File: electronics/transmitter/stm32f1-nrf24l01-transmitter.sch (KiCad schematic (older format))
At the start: 34 parts, among them K1 CONN_3, K10 CONN_3, K11 CONN_3, K12 UART, K2 CONN_3, K3 CONN_3, K4 CONN_3, K5 CONN_3, K6 CONN_3, K7 CONN_3, K8 CONN_3, K9 CONN_3, P1 Charge, P2 LED, P3 PWR-BAT, P4 PWR-IN, P5 Buzzer, P6 Meter, Q1 BC547B, SW1 ON/OFF, U1 LIPO_CHARGER_+_PROTECTION, U2 STM32F103C8T6_DEV_BOARD, U3 NRF24L01P

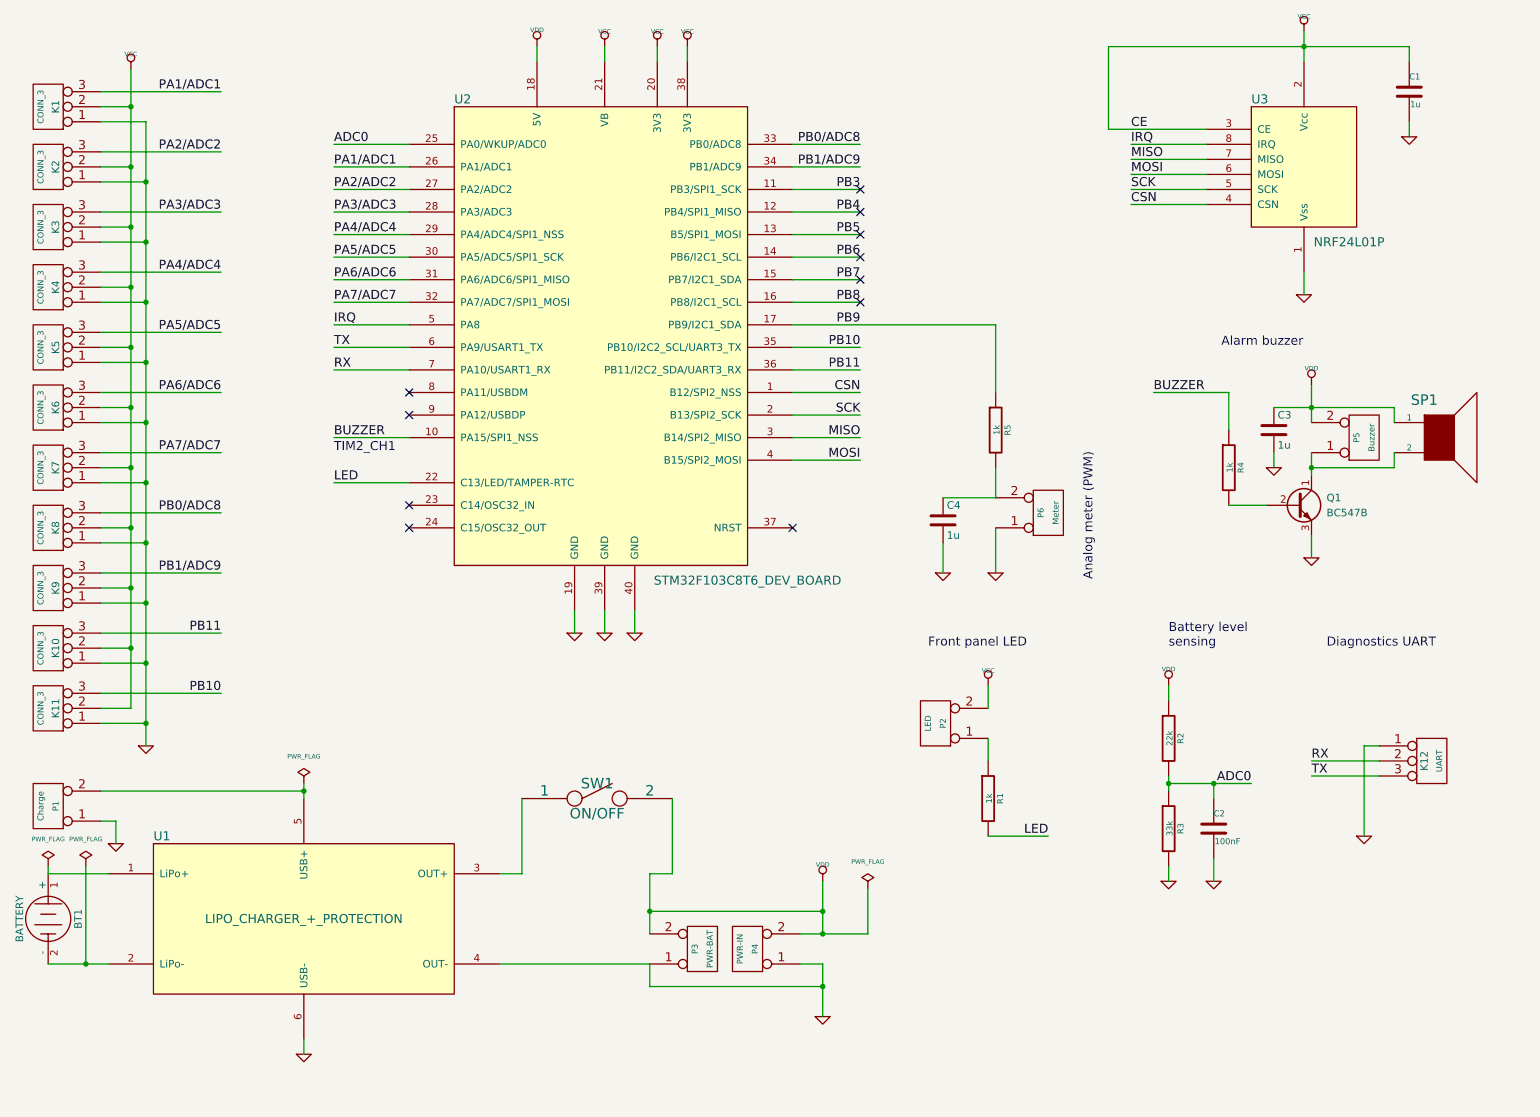
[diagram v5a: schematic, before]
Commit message: Add info about Airtronics meter
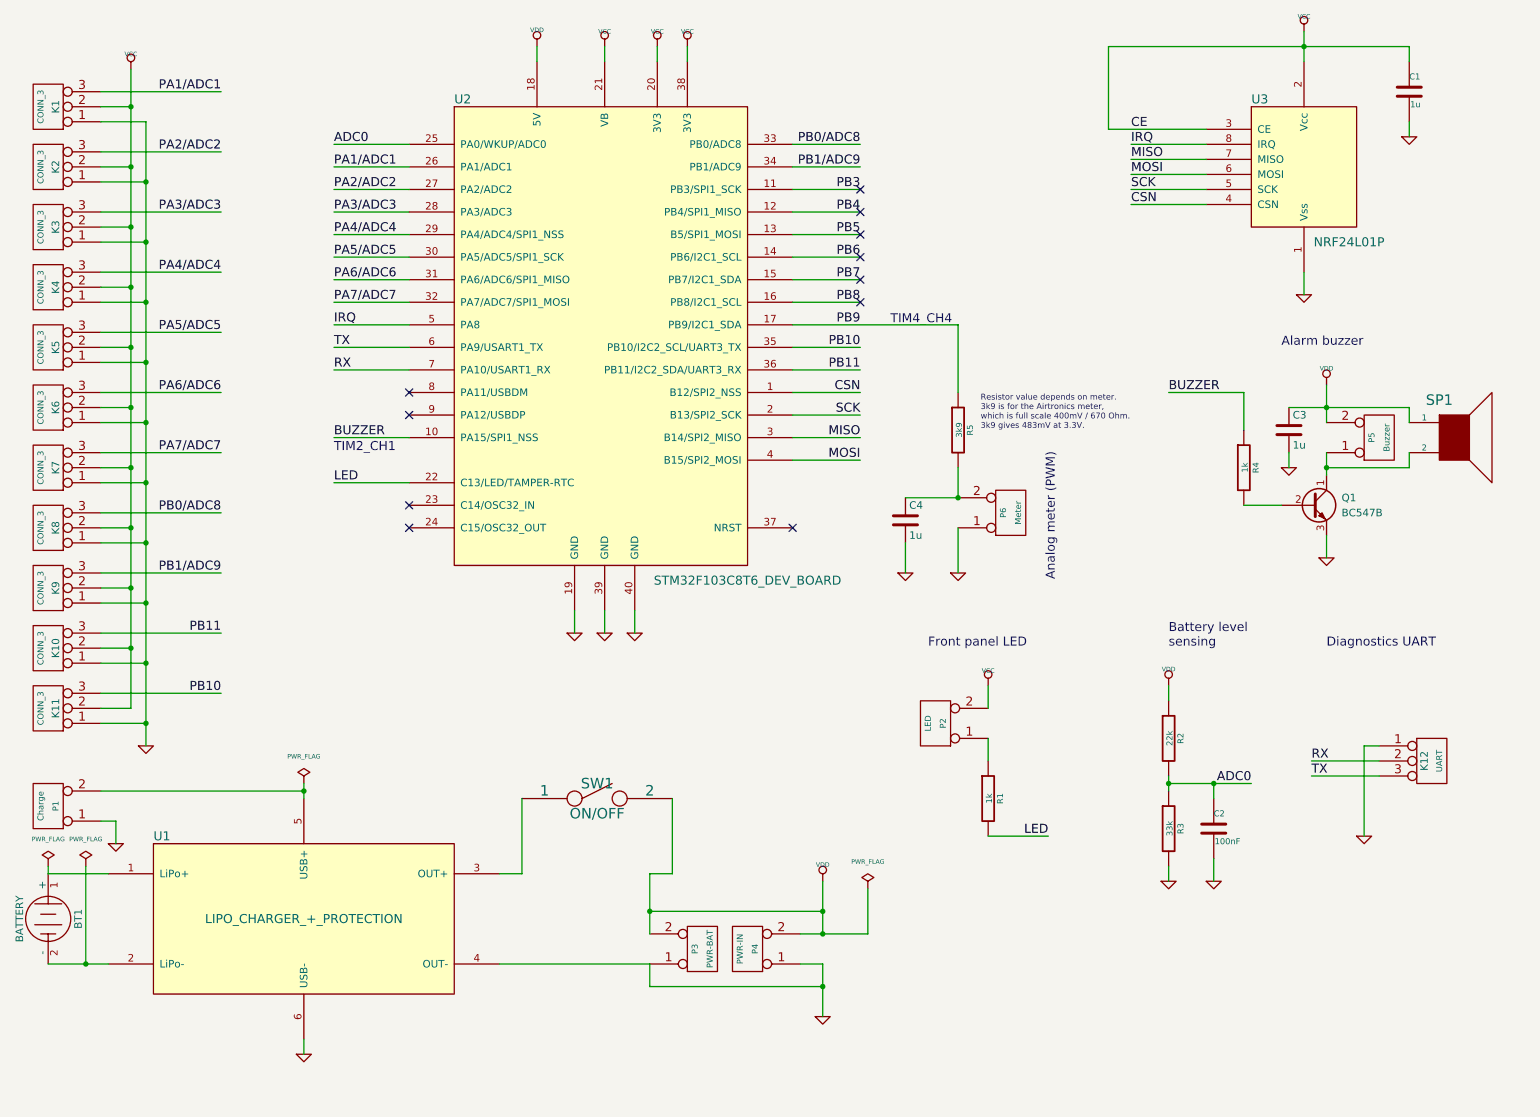
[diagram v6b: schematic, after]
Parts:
- R5: value 1k -> 3k9
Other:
- note added: "Resistor value depends on meter. \n3k9 is for the Airtronics meter, \nwhich is full scale 400mV / 670 Ohm.\n3k9 gives 483mV at 3.3V."
- note added: "TIM4_CH4"
- moved on the sheet: C3, C4, P5, P6, Q1, R4, R5, SP1

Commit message: Remove values on connectors, fix-up meter resistor
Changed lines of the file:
@@
 	10350 1350 10350 1450
 Wire Wire Line
-	9650 750  9650 850
-Wire Wire Line
-	9650 850  9650 950
+	9650 750  9650 950
 Wire Wire Line
 	10350 850  10350 950
@@
 	8750 5100 8750 5200
 Wire Wire Line
-	8750 5700 8750 5750
-Wire Wire Line
-	8750 5750 8750 5800
+	8750 5700 8750 5800
 Wire Wire Line
 	8750 6300 8750 6400
 Wire Wire Line
-	8750 5750 9050 5750
-Wire Wire Line
-	9050 5750 9300 5750
+	8750 5750 9300 5750
 Connection ~ 8750 5750
 Wire Wire Line
@@
 	1950 5350 1650 5350
 Wire Wire Line
-	1950 1350 1950 1750
-Wire Wire Line
-	1950 1750 1950 2150
-Wire Wire Line
-	1950 2150 1950 2550
-Wire Wire Line
-	1950 2550 1950 2950
-Wire Wire Line
-	1950 2950 1950 3350
-Wire Wire Line
-	1950 3350 1950 3750
-Wire Wire Line
-	1950 3750 1950 4150
-Wire Wire Line
-	1950 4150 1950 4550
-Wire Wire Line
-	1950 4550 1950 4950
-Wire Wire Line
-	1950 4950 1950 5350
-Wire Wire Line
-	1950 5350 1950 5500
+	1950 1350 1950 5500
 Wire Wire Line
 	1650 4950 1950 4950
@@
 	9800 4100 9800 4250
 Wire Wire Line
-	9800 3550 9800 3650
-Wire Wire Line
-	9800 3650 9800 3700
+	9800 3550 9800 3700
 Wire Wire Line
 	9250 3900 9500 3900
@@
 	9250 3150 8750 3150
 Wire Wire Line
-	9800 3100 9800 3250
-Wire Wire Line
-	9800 3250 9800 3350
+	9800 3100 9800 3350
 Wire Wire Line
 	3200 3450 3700 3450
@@
 	1650 5800 3000 5800
 Wire Wire Line
-	3000 5750 3000 5800
-Wire Wire Line
-	3000 5800 3000 5850
-Wire Wire Line
-	1300 6950 1550 6950
-Wire Wire Line
-	1550 6950 1700 6950
+	3000 5750 3000 5850
+Wire Wire Line
+	1300 6950 1700 6950
 Wire Wire Line
 	1300 6350 1700 6350
@@
 	1850 5250 1650 5250
 Wire Wire Line
-	1850 1000 1850 1250
-Wire Wire Line
-	1850 1250 1850 1650
-Wire Wire Line
-	1850 1650 1850 2050
-Wire Wire Line
-	1850 2050 1850 2450
-Wire Wire Line
-	1850 2450 1850 2850
-Wire Wire Line
-	1850 2850 1850 3250
-Wire Wire Line
-	1850 3250 1850 3650
-Wire Wire Line
-	1850 3650 1850 4050
-Wire Wire Line
-	1850 4050 1850 4450
-Wire Wire Line
-	1850 4450 1850 4850
-Wire Wire Line
-	1850 4850 1850 5250
+	1850 1000 1850 5250
 Wire Wire Line
 	1650 4850 1850 4850
@@
 Connection ~ 1850 1250
 Wire Wire Line
-	6300 6750 6450 6750
-Wire Wire Line
-	6450 6750 6750 6750
-Wire Wire Line
-	6450 6400 6450 6600
-Wire Wire Line
-	6450 6600 6450 6750
+	6300 6750 6750 6750
+Wire Wire Line
+	6450 6400 6450 6750
 Wire Wire Line
 	6300 6950 6450 6950
 Wire Wire Line
-	6450 6950 6450 7100
-Wire Wire Line
-	6450 7100 6450 7300
+	6450 6950 6450 7300
 Wire Wire Line
 	6750 6750 6750 6450
@@
 	5450 6350 5300 6350
 Wire Wire Line
-	5300 6350 5300 6600
-Wire Wire Line
-	5300 6600 5300 6750
+	5300 6350 5300 6750
 Wire Wire Line
 	5550 850  5550 950
 Wire Wire Line
-	8350 850  9650 850
-Wire Wire Line
-	9650 850  10350 850
+	8350 850  10350 850
 Wire Wire Line
 	8350 850  8350 1400
@@
 Connection ~ 6450 7100
 Wire Wire Line
-	9550 3250 9800 3250
-Wire Wire Line
-	9800 3250 10350 3250
+	9550 3250 10350 3250
 Wire Wire Line
 	10350 3250 10350 3350
@@
 $EndComp
 $Comp
-L VCC #PWR?
+L VCC #PWR030
 U 1 1 58D2422E
 P 5350 850
-F 0 "#PWR?" H 5350 950 30  0001 C CNN
+F 0 "#PWR030" H 5350 950 30  0001 C CNN
 F 1 "VCC" H 5350 950 30  0000 C CNN
 F 2 "" H 5350 850 60  0000 C CNN
